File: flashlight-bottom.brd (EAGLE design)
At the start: 33.1 x 17.8 mm, 0 parts

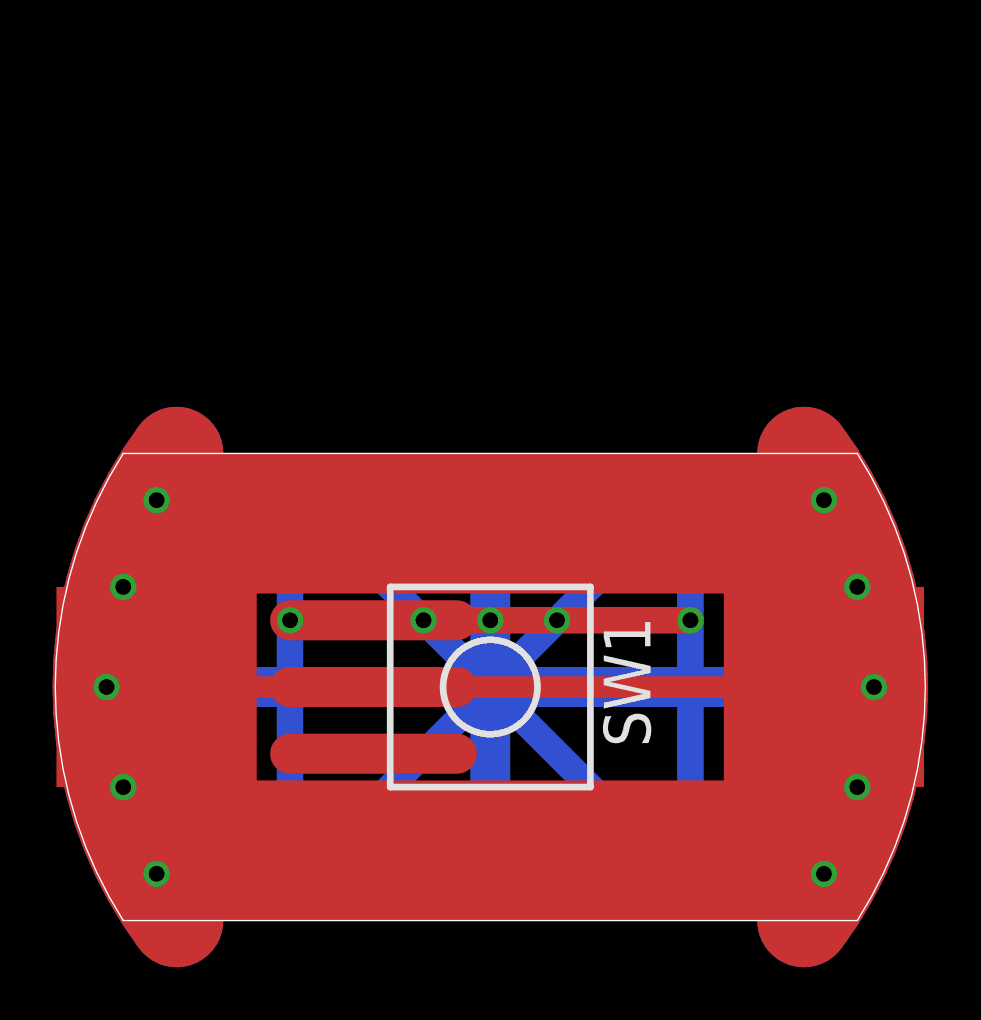
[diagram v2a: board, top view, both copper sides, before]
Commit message: make unused switch pad act same as middle pad
this allows switches with just two pins in the same place as the
outer pads work
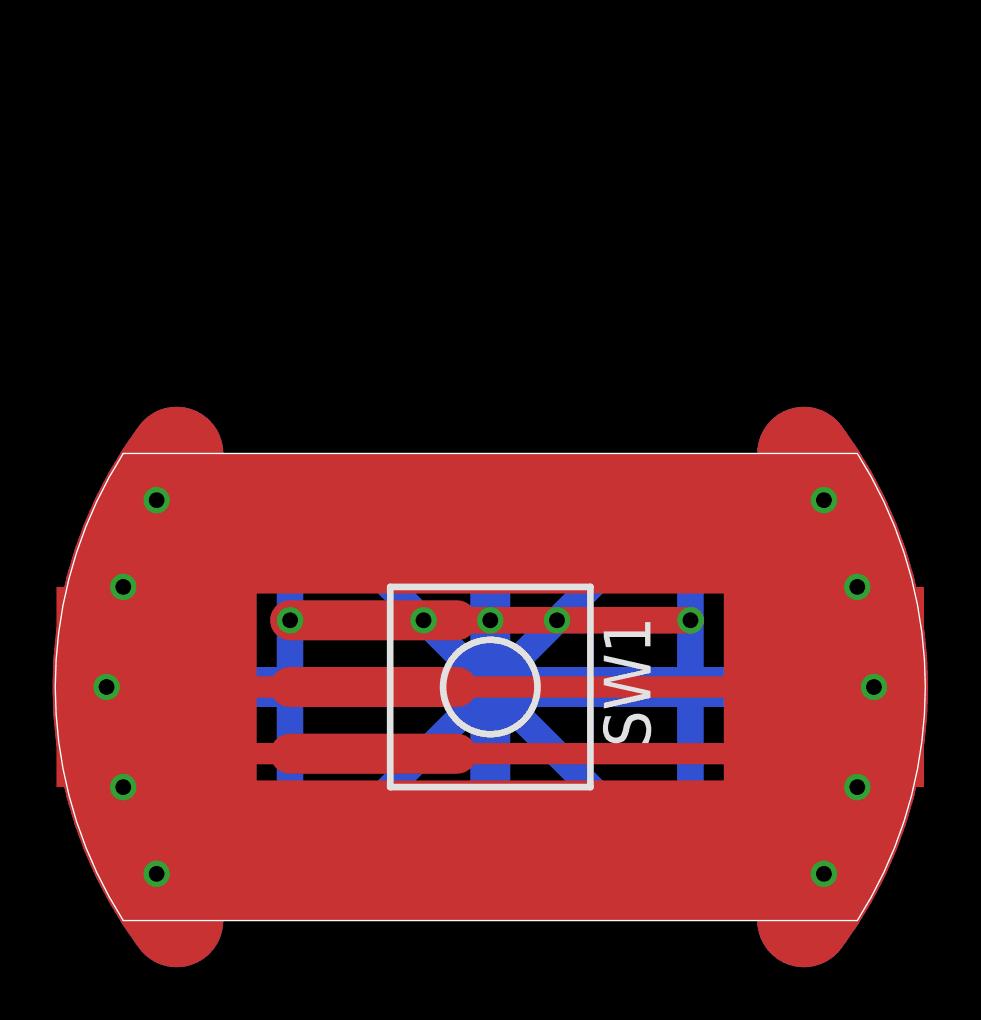
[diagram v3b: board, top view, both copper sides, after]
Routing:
- net N$3: track 0.00 -> 20.3 mm
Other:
- board text added: "Bottom Board Rev. 3.1"
- board text removed: "Bottom Board Rev. 3.0"
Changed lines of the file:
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@@
 Flashlight</text>
 <text x="16.51" y="0.508" size="1.778" layer="29" align="bottom-center">Bottom Board
-Rev. 3.0</text>
+Rev. 3.1</text>
 <wire x1="16.51" y1="8.89" x2="8.89" y2="16.51" width="1.016" layer="30"/>
 <wire x1="16.51" y1="8.89" x2="5.08" y2="8.89" width="1.524" layer="30"/>
@@
 <wire x1="8.89" y1="11.43" x2="15.24" y2="11.43" width="1.524" layer="1"/>
 </signal>
+<signal name="N$3">
+<wire x1="6.35" y1="6.35" x2="26.67" y2="6.35" width="0.8128" layer="1"/>
+</signal>
 </signals>
